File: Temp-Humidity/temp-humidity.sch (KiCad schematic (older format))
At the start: 29 parts, among them IC1 ATMEGA328P-A, P1 +BATT, P2 -BATT, P3 NRF24L01, P4 CONN_02X03, P5 SERIAL/DEBUG, U2 AT25DF512, U3 HDC1080, U4 ATSHA204A, Y1 12MHz

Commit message: Update Debug 3v3 detection
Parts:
- added Q?: Q_PMOS_GSD, symbol Q_PMOS_GSD
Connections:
- wire segments 128 -> 168
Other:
- note added: "VBAT : 1.8v -> 3v"
- note removed: "VBAT : 1v -> 3v"
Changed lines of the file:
@@
 	7000 1700 7300 1700
 Wire Wire Line
-	6600 1400 6600 1500
+	6600 1400 6600 1450
+Wire Wire Line
+	6600 1450 6600 1500
 Wire Wire Line
 	6600 2100 6600 2200
@@
 	6200 2800 6100 2800
 Wire Wire Line
-	6100 2800 6100 3000
+	6100 2800 6100 2950
+Wire Wire Line
+	6100 2950 6100 3000
 Wire Wire Line
 	6100 2700 6200 2700
 Wire Wire Line
-	6100 2550 6100 2700
+	6100 2550 6100 2600
+Wire Wire Line
+	6100 2600 6100 2700
 Wire Wire Line
 	6200 3550 6100 3550
@@
 	6200 1700 6100 1700
 Wire Wire Line
-	6100 1450 6100 1800
-Wire Wire Line
-	5900 1450 6600 1450
+	6100 1450 6100 1700
+Wire Wire Line
+	6100 1700 6100 1800
+Wire Wire Line
+	5900 1450 6100 1450
+Wire Wire Line
+	6100 1450 6600 1450
 Connection ~ 6600 1450
 Wire Wire Line
@@
 Connection ~ 6100 1700
 Wire Wire Line
-	5650 1900 6200 1900
-Wire Wire Line
-	7100 2800 7600 2800
+	5650 1900 5900 1900
+Wire Wire Line
+	5900 1900 6200 1900
+Wire Wire Line
+	7100 2800 7250 2800
+Wire Wire Line
+	7250 2800 7500 2800
+Wire Wire Line
+	7500 2800 7600 2800
 Wire Wire Line
 	7250 2800 7250 3550
@@
 	7250 3550 7100 3550
 Wire Wire Line
-	7100 2700 7600 2700
+	7100 2700 7350 2700
+Wire Wire Line
+	7350 2700 7600 2700
 Connection ~ 7250 2800
 Wire Wire Line
@@
 	7350 2400 7350 2350
 Wire Wire Line
-	7350 2350 7500 2350
+	7350 2350 7450 2350
+Wire Wire Line
+	7450 2350 7500 2350
 Wire Wire Line
 	7500 2350 7500 2400
@@
 	5000 2450 5000 2300
 Wire Wire Line
-	5000 2300 5250 2300
+	5000 2300 5200 2300
+Wire Wire Line
+	5200 2300 5250 2300
 Wire Wire Line
 	5200 2300 5200 2400
@@
 	5000 2550 5000 2700
 Wire Wire Line
-	5000 2700 5250 2700
+	5000 2700 5200 2700
+Wire Wire Line
+	5200 2700 5250 2700
 Wire Wire Line
 	5200 2700 5200 2600
@@
 	2400 1850 1700 1850
 Wire Wire Line
-	1700 1700 1700 2750
+	1700 1700 1700 1850
+Wire Wire Line
+	1700 1850 1700 1950
+Wire Wire Line
+	1700 1950 1700 2150
+Wire Wire Line
+	1700 2150 1700 2750
 Wire Wire Line
 	1700 1950 2400 1950
 Connection ~ 1700 1850
 Wire Wire Line
-	1700 2150 2400 2150
+	1700 2150 1950 2150
+Wire Wire Line
+	1950 2150 2400 2150
 Connection ~ 1700 1950
 Wire Wire Line
 	1700 4150 2400 4150
 Wire Wire Line
-	1700 2950 1700 4200
-Wire Wire Line
-	1700 4050 2400 4050
+	1700 2950 1700 4050
+Wire Wire Line
+	1700 4050 1700 4150
+Wire Wire Line
+	1700 4150 1700 4200
+Wire Wire Line
+	1700 4050 1950 4050
+Wire Wire Line
+	1950 4050 2200 4050
+Wire Wire Line
+	2200 4050 2400 4050
 Connection ~ 1700 4150
 Wire Wire Line
@@
 	2400 3950 2200 3950
 Wire Wire Line
-	2200 2950 2200 4050
+	2200 2950 2200 3950
+Wire Wire Line
+	2200 3950 2200 4050
 Connection ~ 1700 2150
 Wire Wire Line
@@
 	7000 4450 6900 4450
 Wire Wire Line
-	7000 4200 7000 4450
+	7000 4200 7000 4250
+Wire Wire Line
+	7000 4250 7000 4450
 Wire Wire Line
 	6400 4450 6300 4450
 Wire Wire Line
-	6300 4250 6300 4900
+	6300 4250 6300 4450
+Wire Wire Line
+	6300 4450 6300 4900
 Wire Wire Line
 	6400 4550 6150 4550
@@
 SCK
 Wire Wire Line
-	8950 2100 9150 2100
+	8950 2100 9100 2100
+Wire Wire Line
+	9100 2100 9150 2100
 Text Label 8950 2100 2    60   ~ 0
 RESET
@@
 	9400 2950 9200 2950
 Wire Wire Line
-	9200 2950 9200 3550
+	9200 2950 9200 3050
+Wire Wire Line
+	9200 3050 9200 3550
 Wire Wire Line
 	9400 3050 9200 3050
@@
 	9400 3150 9300 3150
 Wire Wire Line
-	9300 2850 9300 4150
+	9300 2850 9300 3150
+Wire Wire Line
+	9300 3150 9300 4150
 Wire Wire Line
 	9400 3250 9100 3250
@@
 	5350 5600 5050 5600
 Wire Wire Line
-	5350 5050 5350 5800
+	5350 5050 5350 5200
+Wire Wire Line
+	5350 5200 5350 5600
+Wire Wire Line
+	5350 5600 5350 5800
 $Comp
 L D D1
@@
 Connection ~ 5350 5200
 Wire Wire Line
-	3900 5500 4250 5500
+	3900 5500 4150 5500
+Wire Wire Line
+	4150 5500 4250 5500
 Wire Wire Line
 	4150 5500 4150 5200
@@
 $EndComp
 Wire Wire Line
-	1900 5950 1900 6100
-Wire Wire Line
-	1450 5500 2250 5500
-Wire Wire Line
-	1900 5050 1900 5750
+	1900 5950 1900 6050
+Wire Wire Line
+	1900 6050 1900 6100
+Wire Wire Line
+	1450 5500 1900 5500
+Wire Wire Line
+	1900 5500 2250 5500
+Wire Wire Line
+	1900 5050 1900 5500
+Wire Wire Line
+	1900 5500 1900 5750
 Connection ~ 1900 5500
 Text Label 1550 5500 2    60   ~ 0
 VIN
 Text Notes 750  5850 0    60   ~ 0
-VBAT : 1v -> 3v
+VBAT : 1.8v -> 3v
 $Comp
 L CONN_01X01 P1
@@
 $EndComp
 Wire Wire Line
-	1450 6050 2200 6050
+	1450 6050 1900 6050
+Wire Wire Line
+	1900 6050 2050 6050
+Wire Wire Line
+	2050 6050 2200 6050
 Connection ~ 1900 6050
 Text Notes 5500 5150 0    60   ~ 0
@@
 	5450 2300 5550 2300
 Wire Wire Line
-	5550 2300 5550 2700
+	5550 2300 5550 2500
+Wire Wire Line
+	5550 2500 5550 2700
 Wire Wire Line
 	5550 2700 5450 2700
@@
 Text Notes 2250 6050 0    60   ~ 0
 22k arround 1min
+$Comp
+L Q_PMOS_GSD Q?
+U 1 1 58380B3A
+P 9950 5250
+F 0 "Q?" H 10250 5300 50  0000 R CNN
+F 1 "Q_PMOS_GSD" H 10600 5200 50  0000 R CNN
+F 2 "" H 10150 5350 50  0000 C CNN
+F 3 "" H 9950 5250 50  0000 C CNN
+	1    9950 5250
+	0    1    1    0
+$EndComp
+$Comp
+L VDD #PWR?
+U 1 1 58380C33
+P 9950 4950
+F 0 "#PWR?" H 9950 4800 50  0001 C CNN
+F 1 "VDD" H 9950 5100 50  0000 C CNN
+F 2 "" H 9950 4950 50  0000 C CNN
+F 3 "" H 9950 4950 50  0000 C CNN
+	1    9950 4950
+	1    0    0    -1
+$EndComp
+$Comp
+L +BATT #PWR?
+U 1 1 58380CF2
+P 9550 5250
+F 0 "#PWR?" H 9550 5100 50  0001 C CNN
+F 1 "+BATT" H 9550 5390 50  0000 C CNN
+F 2 "" H 9550 5250 50  0000 C CNN
+F 3 "" H 9550 5250 50  0000 C CNN
+	1    9550 5250
+	1    0    0    -1
+$EndComp
+$Comp
+L +3.3V #PWR?
+U 1 1 58380D57
+P 10300 5250
+F 0 "#PWR?" H 10300 5100 50  0001 C CNN
+F 1 "+3.3V" H 10300 5390 50  0000 C CNN
+F 2 "" H 10300 5250 50  0000 C CNN
+F 3 "" H 10300 5250 50  0000 C CNN
+	1    10300 5250
+	1    0    0    -1
+$EndComp
+Wire Wire Line
+	9950 4950 9950 5050
+Wire Wire Line
+	9750 5350 9550 5350
+Wire Wire Line
+	9550 5350 9550 5250
+Wire Wire Line
+	10150 5350 10300 5350
+Wire Wire Line
+	10300 5350 10300 5250
 $EndSCHEMATC

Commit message: Add switch for 3v3 / Serial debug port alimentation and use Timer mode for TPL5110
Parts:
- removed C5: CP1_Small, symbol CP1_Small
- removed Q? (x2): Q_PMOS_GSD, symbol Q_PMOS_GSD
- added C10, C5: 22uF, symbol C_Small
- added JP1: Jumper_NO_Small, symbol Jumper_NO_Small
- added R6: 48.7k, Resistors_SMD:R_0805_HandSoldering, symbol R_Small
- L1: value INDUCTOR_SMALL -> 47uF
- R5: renamed from R?; value 22k -> 40.2k
- gave numbers to parts that had none: 5
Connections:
- wire segments 168 -> 177
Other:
- note added: "1min : 40.2 // 48.7\n"
- note added: "Schottky diode VF < 0.3V"
- note removed: "22k arround 1min"
- moved on the sheet: C3, L1, P1, P2

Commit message: Update schematics
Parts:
- D1: value D -> MBR0520LT1G; footprint (none) -> Diodes_SMD:SOD-123
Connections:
- wire segments 177 -> 134

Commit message: More work on hum/temp sensor
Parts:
- removed P1: +BATT, Pin_Headers:Pin_Header_Straight_1x01, symbol CONN_01X01
- removed R1: 4k7, Resistors_SMD:R_0805_HandSoldering, symbol R_Small
- removed R2, R3: R_Small, Resistors_SMD:R_0805_HandSoldering, symbol R_Small
- removed R4: 10k, Resistors_SMD:R_0805_HandSoldering, symbol R_Small
- removed R5: 40.2k, Resistors_SMD:R_0805_HandSoldering, symbol R_Small
- removed R6: 48.7k, Resistors_SMD:R_0805_HandSoldering, symbol R_Small
- added D?: LED_RABG, symbol LED_RABG
- added P1: BATTERY, Connectors_JST:JST_PH_S2B-PH-K_02x2.00mm_Angled, symbol CONN_01X02
- added R1: 40k2, Resistors_SMD:R_0805_HandSoldering, symbol R
- added R2: 48k7, Resistors_SMD:R_0805_HandSoldering, symbol R
- added R3, R4, R5, R6: 4k7, Resistors_SMD:R_0805_HandSoldering, symbol R
- added R7: 10k, Resistors_SMD:R_0805_HandSoldering, symbol R
- added R?: 160, symbol R
- added U6: RFM69HW, kicad-libraries:RFM69HW, symbol RFM69HW
- C10, C3, C4, C5, C6, C7, C8, C9: footprint (none) -> Capacitors_SMD:C_0805_HandSoldering
- IC1: footprint TQFP32 -> Housings_QFP:TQFP-32_7x7mm_Pitch0.8mm
- JP1: footprint (none) -> Pin_Headers:Pin_Header_Straight_1x02
- P2: value -BATT -> ANTENNA; footprint Pin_Headers:Pin_Header_Straight_1x01 -> Measurement_Points:Measurement_Point_Round-TH_Big
- U1: footprint (none) -> TO_SOT_Packages_SMD:SOT-23-6_Handsoldering
- U3: footprint (none) -> TO_SOT_Packages_SMD:SC-70-6
- U5: footprint (none) -> TO_SOT_Packages_SMD:SOT-23-5
- Y1: footprint (none) -> Crystals:Crystal_MC-156
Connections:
- net labels added: CE, CSN, IRQ
- net labels removed: PB1, PB2, PD2, VIN
- wire segments 134 -> 206
- no-connect marks 0 -> 13
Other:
- note added: "1 minute : 40.2 // 48.7\n"
- note removed: "1min : 40.2 // 48.7\n"

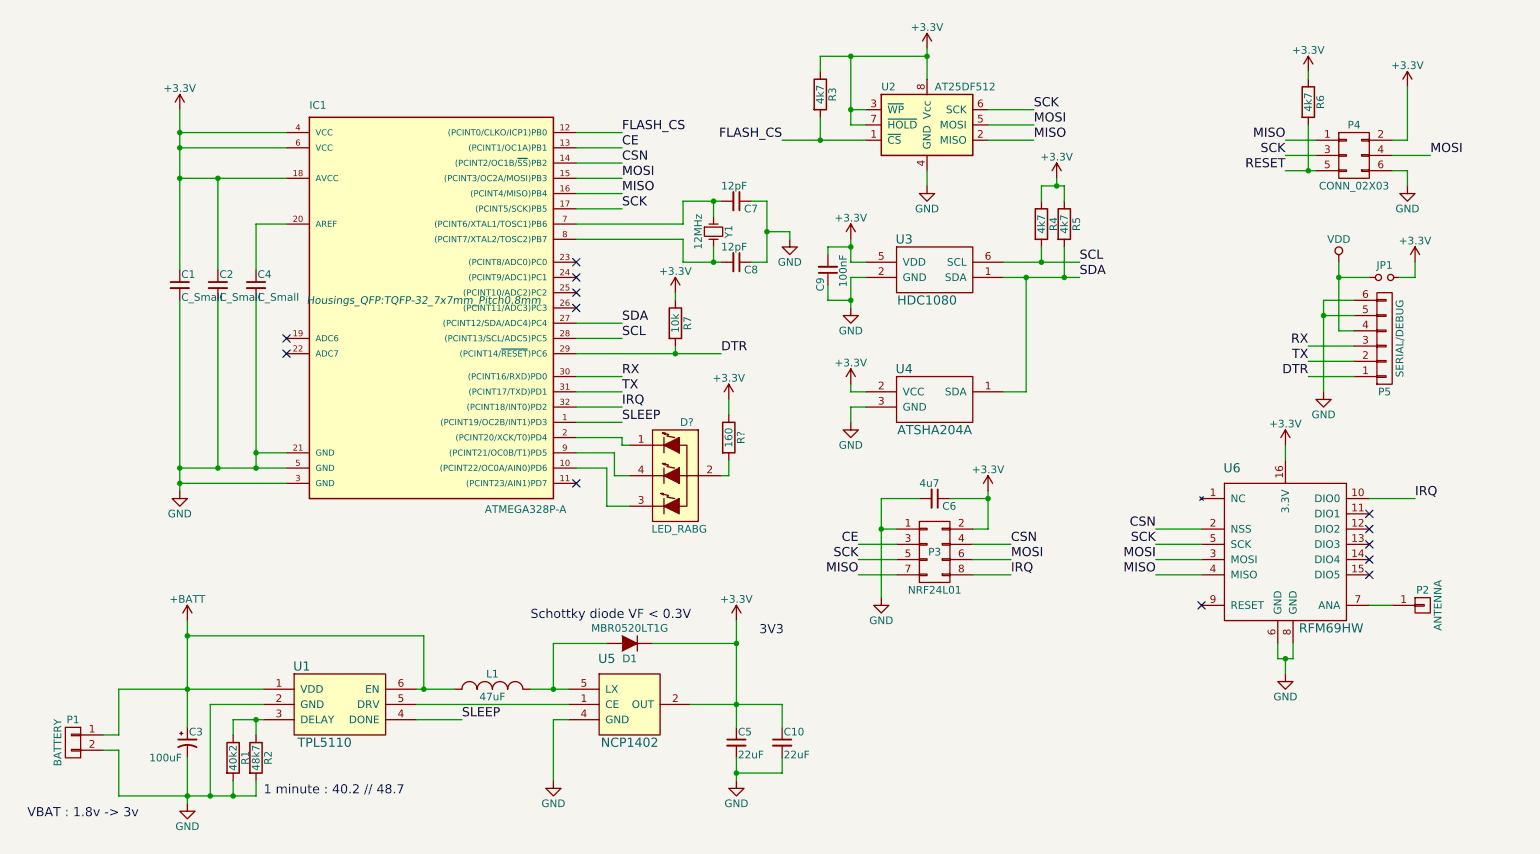
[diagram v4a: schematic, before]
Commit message: Remove alimentation
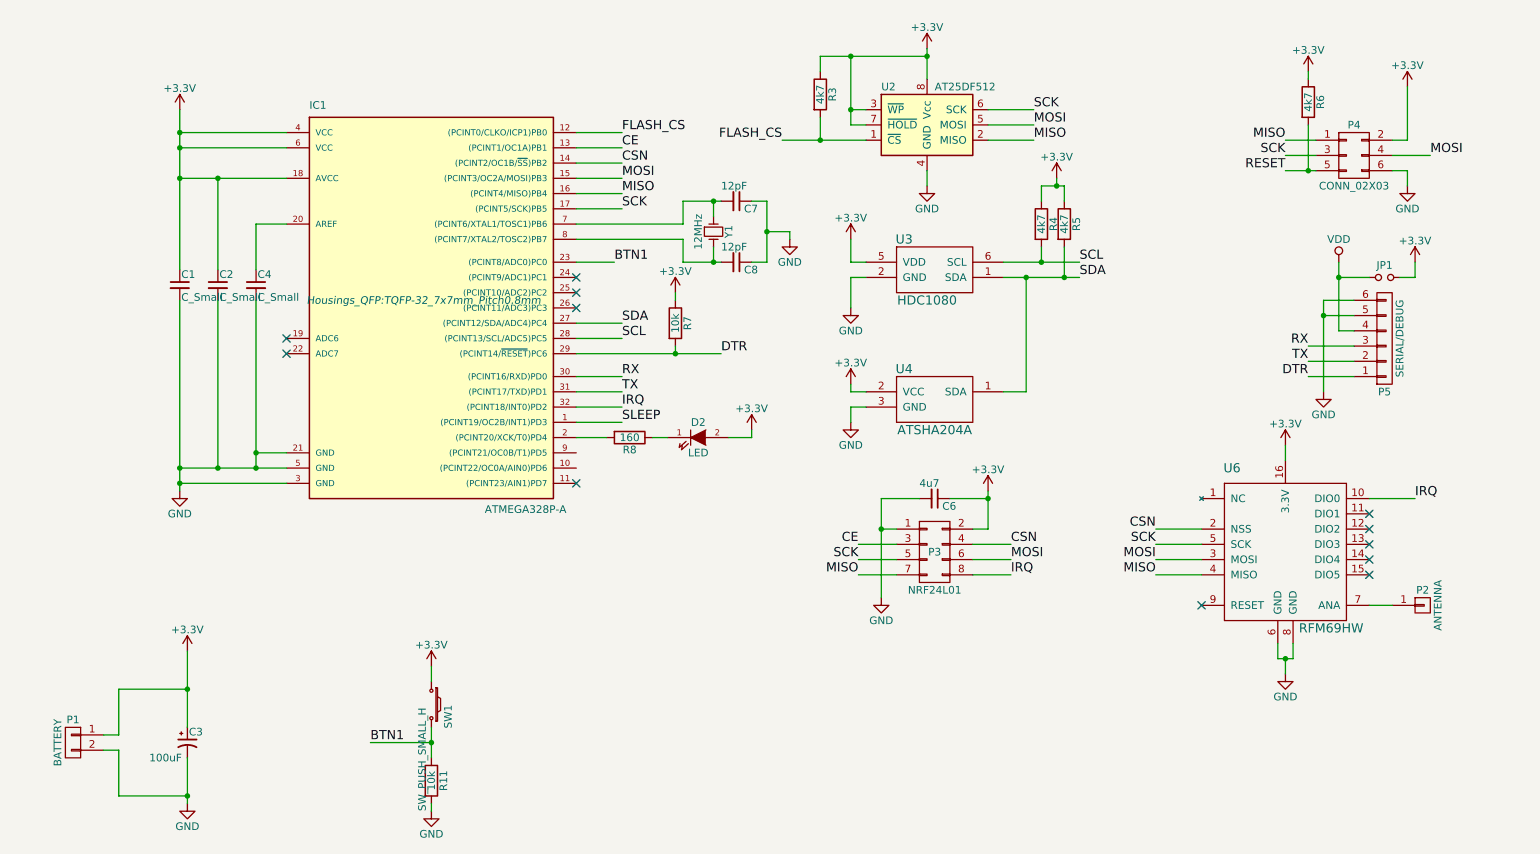
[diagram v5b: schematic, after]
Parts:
- removed C10, C5: 22uF, Capacitors_SMD:C_0805_HandSoldering, symbol C_Small
- removed C9: 100nF, Capacitors_SMD:C_0805_HandSoldering, symbol C_Small
- removed D1: MBR0520LT1G, Diodes_SMD:SOD-123, symbol D
- removed D?: LED_RABG, symbol LED_RABG
- removed L1: 47uF, Inductors:Inductor_1212, symbol INDUCTOR_SMALL
- removed R1: 40k2, Resistors_SMD:R_0805_HandSoldering, symbol R
- removed R2: 48k7, Resistors_SMD:R_0805_HandSoldering, symbol R
- removed U1: TPL5110, TO_SOT_Packages_SMD:SOT-23-6_Handsoldering, symbol TPL5110
- removed U5: NCP1402, TO_SOT_Packages_SMD:SOT-23-5, symbol NCP1402
- added D2: LED, LEDs:LED_0805, symbol LED
- added R11: 10k, Resistors_SMD:R_0805_HandSoldering, symbol R
- added SW1: SW_PUSH_SMALL_H, kicad-libraries:SW_06_SMD, symbol SW_PUSH_SMALL_H
- R8: renamed from R?; footprint (none) -> Resistors_SMD:R_0805_HandSoldering
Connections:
- net +BATT is gone; now on net +3V3: C3.1, P1.1 (P1)
- net +3V3: now also D2.2 (A), SW1.1; no longer R8.1
- net GND: now also R11.2
- net at IC1.2 ((PCINT20/XCK/T0)PD4): now also R8.2
- net BTN1: now reaches IC1.23 ((PCINT8/ADC0)PC0)
- net BTN1: now also R11.1, SW1.2
- new net: D2.1 (K), R8.1
- no-connect marks 13 -> 12
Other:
- note removed: "1 minute : 40.2 // 48.7\n"
- note removed: "3V3"
- note removed: "Schottky diode VF < 0.3V"
- note removed: "VBAT : 1.8v -> 3v"
- moved on the sheet: R8

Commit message: More work on pcb, but bad cutting edges
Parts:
- removed C6: 4u7, Capacitors_SMD:C_0805_HandSoldering, symbol C_Small
- removed P3: NRF24L01, Pin_Headers:Pin_Header_Straight_2x04, symbol CONN_02X04
- added C7: 4u7, Capacitors_SMD:C_0805_HandSoldering, symbol C_Small
- added U4: NRF24L01, mysensors_radios:NRF24L01-SMD, symbol NRF24L01
- U5: renamed from U6; footprint kicad-libraries:RFM69HW -> mysensors_radios:RFM69HW_SMD
- Y1: footprint Crystals:Crystal_MC-156 -> Crystals:Crystal_SMD_5032_2Pads
- renumbered C3 to C2, C2 to C3, C7 to C5, C8 to C6, D2 to D1, P4 to P2, P5 to P3, P2 to P4, R11 to R1, R8 to R2, R7 to R3, R3 to R4, R4 to R5, R5 to R6, R6 to R7, U2 to U1, U3 to U2, U4 to U3
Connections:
- net +3V3: now also P1.2 (P2), C7.1, U4.2 (VCC); no longer P1.1 (P1)
- net CE: now also U4.3 (CE)
- net CSN: now also U4.4 (CSN)
- net GND: now also P1.1 (P1), C7.2, U4.1 (GND); no longer P1.2 (P2)
- net IRQ: now also U4.8 (IRQ)
- net MISO: now also U4.7 (MISO)
- net MOSI: now also U4.6 (MOSI)
- net SCK: now also U4.5 (SCK)

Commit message: More work on hum/temp
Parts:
- Y1: footprint Crystals:Crystal_SMD_5032_2Pads -> mysensors_obscurities:XTAL_3.2x1.5mm
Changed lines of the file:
@@
 LIBS:tinkerforge
 LIBS:mysensors_radios
+LIBS:mysensors_sensors
 LIBS:temp-humidity-cache
 EELAYER 25 0
@@
 F 0 "Y1" H 5200 2600 50  0000 C CNN
 F 1 "12MHz" H 5200 2400 50  0000 C CNN
-F 2 "Crystals:Crystal_SMD_5032_2Pads" H 5200 2500 50  0001 C CNN
+F 2 "mysensors_obscurities:XTAL_3.2x1.5mm" H 5200 2500 50  0001 C CNN
 F 3 "" H 5200 2500 50  0000 C CNN
 	1    5200 2500

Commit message: work++
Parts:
- P3: symbol CONN_01X06 -> CONN_01X06-RESCUE-temp-humidity
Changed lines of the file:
@@
 EESchema Schematic File Version 2
+LIBS:temp-humidity-rescue
 LIBS:power
 LIBS:device
@@
 RESET
 $Comp
-L CONN_01X06 P3
+L CONN_01X06-RESCUE-temp-humidity P3
 U 1 1 58361147
 P 9600 3200
